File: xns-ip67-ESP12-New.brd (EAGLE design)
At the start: 65.3 x 139.1 mm, 86 parts, among them CN2 JSTPH, J1 DCJ0202, U2 MCP73831T-2ACI/OT, X1 ESP-12E

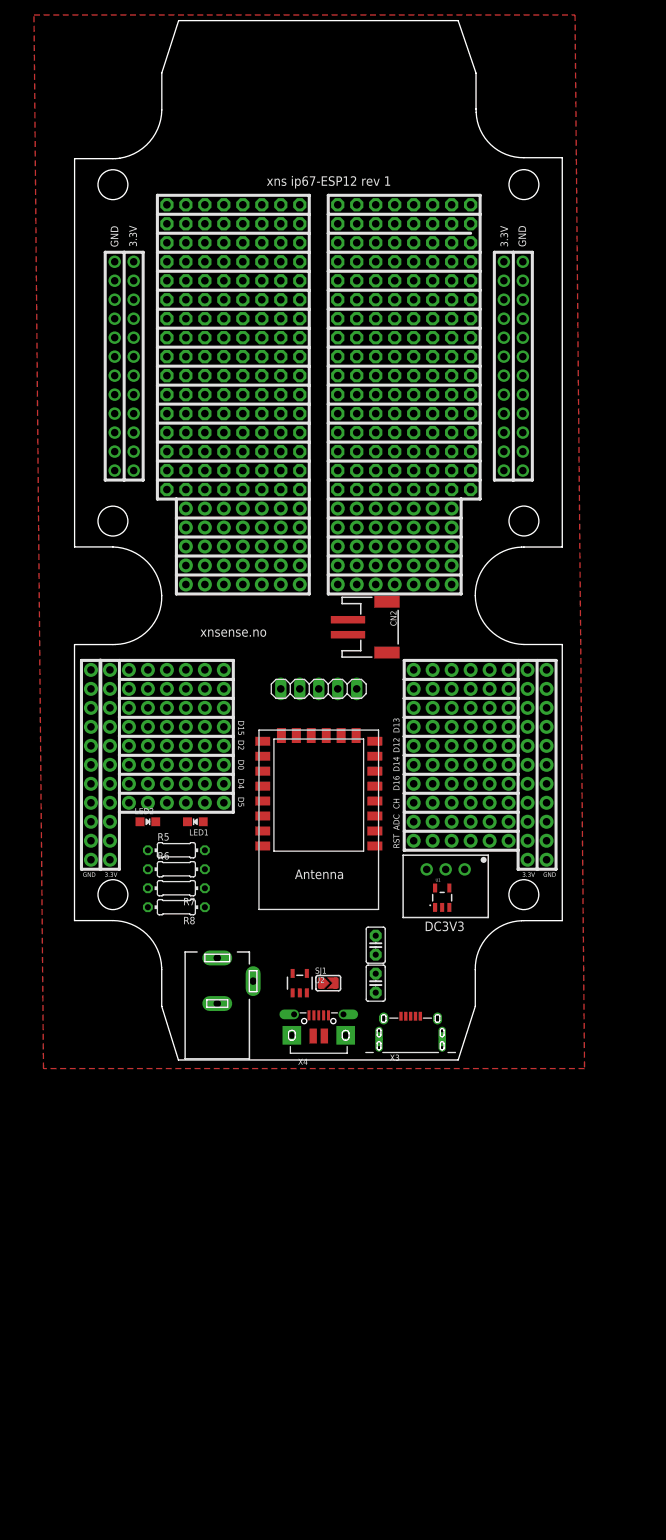
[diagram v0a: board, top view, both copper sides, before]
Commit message: ip67 version with A7, SIM, SMA
Test version with A7, SIM Card Holder and SMA Antenna
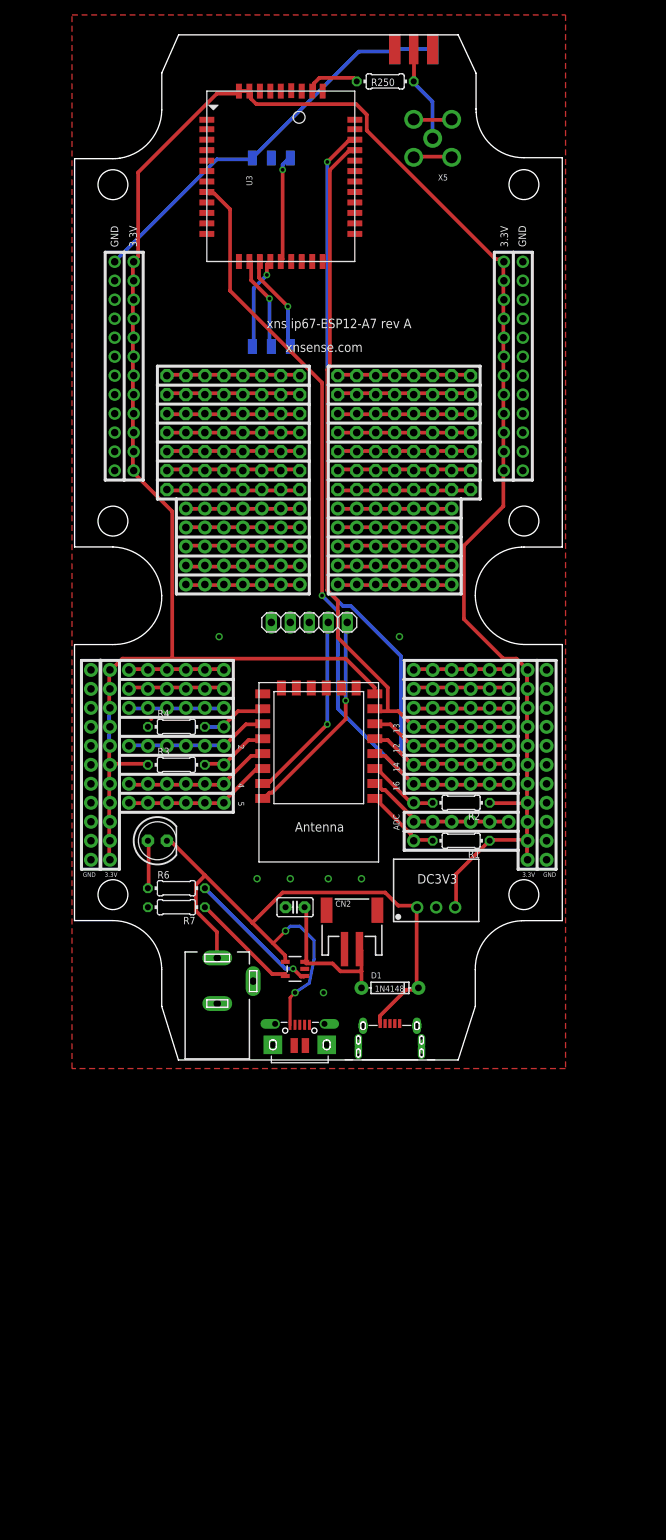
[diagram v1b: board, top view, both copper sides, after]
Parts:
- removed C3: 10uF, capacitor-wima:C2.5-2
- removed J11, J6, J8, J9: (no value), SparkFun-Connectors:1X06_NO_SILK
- removed JP16, JP17, JP18, JP19, JP20, JP21, JP22, JP23, JP24, JP5, JP6, JP7, JP8, JP9: (no value), adafruit:1X08-CLEANBIG
- removed LED1: RED, microbuilder:CHIPLED_0805_NOOUTLINE
- removed LED2: GREEN, microbuilder:CHIPLED_0805_NOOUTLINE
- removed R5: 470, eagle-ltspice:0204/7
- removed R8: 2.5k, eagle-ltspice:0204/7
- removed SJ1: (no value), microbuilder:SOLDERJUMPER_ARROW_NOPASTE
- removed U1: (no value), SparkFun-PowerIC:SOT23-5
- removed X4: (no value), microbuilder:4UCONN_20329_V2
- added D1: 1N4148, SparkFun-DiscreteSemi:DIODE-1N4148
- added JCB_MICROUSB: (no value), jcbrataas-2:USB-MICRO-B
- added LED4: Orange, adafruit:LED5MM
- added R1, R2, R3, R4: 10k, eagle-ltspice:0204/7
- added R250: (no value), eagle-ltspice:0204/7
- added SIMCARD: (no value), SparkFun-Connectors:SIMHOLDER
- added STD_MICROUSB: (no value), microbuilder:4UCONN_20329_V2
- added U3: A7, IC:A7
- added X5: (no value), adafruit:SMA90_DIP
- JP1, JP2, JP3, JP4: device adafruit:1X08-CLEANBIG -> adafruit:1X01-CLEANBIG
- R6: value 470 -> 470k
- X3: device jcbrataas:USB-MICRO-B -> adafruit:SMA_EDGELAUNCH
- moved X3 134.3 mm to (49.5, 138.4), turned to 270 degrees
- moved JP3 83.6 mm to (49.5, 30.5)
- moved JP4 76.3 mm to (49.5, 35.6)
- moved JP1 74.9 mm to (24.1, 40.6)
- moved JP2 67.3 mm to (24.1, 45.7)
- moved CN2 39.5 mm to (41.3, 19.7), turned to 0 degrees
- moved JP25 22.9 mm to (48.3, 80.0)
- moved JP26 22.9 mm to (48.3, 82.5)
- moved JP27 22.9 mm to (48.3, 85.1)
- moved JP28 22.9 mm to (48.3, 87.6)
- moved JP29 22.9 mm to (48.3, 90.2)
- moved JP30 22.9 mm to (48.3, 92.7)
- moved C4 11.9 mm to (33.7, 21.6), turned to 180 degrees
- moved JP37 8.98 mm to (35.6, 59.7)
- moved X1 6.35 mm to (36.8, 41.9)
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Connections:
- net N$13 renamed RX
- net N$4 renamed TX
- removed net N$25: JP5.1, JP5.2, JP5.3, JP5.4, JP5.5, JP5.6, JP5.7, JP5.8
- removed net N$26: JP6.1, JP6.2, JP6.3, JP6.4, JP6.5, JP6.6, JP6.7, JP6.8
- removed net N$27: JP7.1, JP7.2, JP7.3, JP7.4, JP7.5, JP7.6, JP7.7, JP7.8
- removed net N$28: JP8.1, JP8.2, JP8.3, JP8.4, JP8.5, JP8.6, JP8.7, JP8.8
- removed net N$29: JP9.1, JP9.2, JP9.3, JP9.4, JP9.5, JP9.6, JP9.7, JP9.8
- removed net N$42: JP24.1, JP24.2, JP24.3, JP24.4, JP24.5, JP24.6, JP24.7, JP24.8
- removed net N$43: JP22.1, JP22.2, JP22.3, JP22.4, JP22.5, JP22.6, JP22.7, JP22.8
- removed net N$44: JP21.1, JP21.2, JP21.3, JP21.4, JP21.5, JP21.6, JP21.7, JP21.8
- removed net N$45: JP20.1, JP20.2, JP20.3, JP20.4, JP20.5, JP20.6, JP20.7, JP20.8
- removed net N$46: JP19.1, JP19.2, JP19.3, JP19.4, JP19.5, JP19.6, JP19.7, JP19.8
- removed net N$47: JP18.1, JP18.2, JP18.3, JP18.4, JP18.5, JP18.6, JP18.7, JP18.8
- removed net N$48: JP17.1, JP17.2, JP17.3, JP17.4, JP17.5, JP17.6, JP17.7, JP17.8
- removed net N$49: JP16.1, JP16.2, JP16.3, JP16.4, JP16.5, JP16.6, JP16.7, JP16.8
- removed net N$5: J5.1, J5.2, J5.3, J5.4, J5.5, J5.6, X1.4
- removed net N$53: LED1.C, R5.1
- removed net N$57: R7.1, SJ1.2, U2.5
- removed net N$60: R8.1, SJ1.1
- removed net VBAT1: C4.1, CN2.2, U2.3
- removed net VDD: DC3V3.3, J15.1, J15.10, J15.11, J15.2, J15.3, J15.4, J15.5, J15.6, J15.7, J15.8, J15.9, J17.1, J17.10, J17.11, J17.2, J17.3, J17.4, J17.5, J17.6, J17.7, J17.8, J17.9, JP33.1, JP33.10, JP33.11, JP33.12, JP33.2, JP33.3, JP33.4, JP33.5, JP33.6, JP33.7, JP33.8, JP33.9, JP34.1, JP34.10, JP34.11, JP34.12, JP34.2, JP34.3, JP34.4, JP34.5, JP34.6, JP34.7, JP34.8, JP34.9, U1.5, X1.8
- removed net VDD1: C3.1, LED1.A, U2.4, X4.VBUS
- new net 3.3V: DC3V3.3, J15.1, J15.10, J15.11, J15.2, J15.3, J15.4, J15.5, J15.6, J15.7, J15.8, J15.9, J17.1, J17.10, J17.11, J17.2, J17.3, J17.4, J17.5, J17.6, J17.7, J17.8, J17.9, JP33.1, JP33.10, JP33.11, JP33.12, JP33.2, JP33.3, JP33.4, JP33.5, JP33.6, JP33.7, JP33.8, JP33.9, JP34.1, JP34.10, JP34.11, JP34.12, JP34.2, JP34.3, JP34.4, JP34.5, JP34.6, JP34.7, JP34.8, JP34.9, R1.1, R2.1, R3.1, U3.41, U3.42, X1.8
- new net N$13: SIMCARD.C3, U3.15
- new net N$4: X5.GND1, X5.GND2
- new net PWD_KEY: J5.1, J5.2, J5.3, J5.4, J5.5, J5.6, U3.8, X1.4
- new net RESET_KEY: U3.12
- new net UART_RX: J2.1, J2.2, J2.3, J2.4, J2.5, J2.6, U3.30, X1.7
- new net UART_TX: J4.1, J4.2, J4.3, J4.4, J4.5, J4.6, U3.31, X1.5
- new net V_BATT: C4.1, CN2.2, D1.A, U2.3
- net GND: now also JCB_MICROUSB.BL1, JCB_MICROUSB.BL2, JCB_MICROUSB.BL3, JCB_MICROUSB.BL4, JCB_MICROUSB.BR1, JCB_MICROUSB.BR2, JCB_MICROUSB.BR3, JCB_MICROUSB.BR4, JCB_MICROUSB.GND, JCB_MICROUSB.MTL1, JCB_MICROUSB.MTL2, JCB_MICROUSB.MTR1, JCB_MICROUSB.MTR2, R4.1, SIMCARD.C5, STD_MICROUSB.BASE@1, STD_MICROUSB.BASE@2, STD_MICROUSB.GND, STD_MICROUSB.SPRT@1, STD_MICROUSB.SPRT@2, STD_MICROUSB.SPRT@3, STD_MICROUSB.SPRT@4, U3.13, U3.18, U3.22, U3.25, U3.28, U3.34, U3.36, U3.39, U3.40, X3.GND@1, X3.GND@2, X3.GND@3, X3.GND@4; no longer C3.2, LED2.C, R8.2, U1.2, X3.BL1, X3.BL2, X3.BL3, X3.BR1, X3.BR2, X3.BR3, X3.GND, X3.MTL1, X3.MTL2, X3.MTR1, X3.MTR2, X4.BASE@1, X4.BASE@2, X4.GND, X4.SPRT@1, X4.SPRT@2, X4.SPRT@3, X4.SPRT@4
- net N$1: now also R250.1, U3.35; no longer J2.1, J2.2, J2.3, J2.4, J2.5, J2.6, X1.7
- net N$10: now also SIMCARD.C2, U3.14; no longer J9.1, J9.2, J9.3, J9.4, J9.5, J9.6, X1.10
- net N$12: now also JP1.1, R3.2; no longer J11.1, J11.2, J11.3, J11.4, J11.5, J11.6
- net N$21: now also JP3.1, R1.2, X1.1; no longer JP1.1, JP1.2, JP1.3, JP1.4, JP1.5, JP1.6, JP1.7, JP1.8
- net N$22: now also SIMCARD.C7, U3.17; no longer JP2.1, JP2.2, JP2.3, JP2.4, JP2.5, JP2.6, JP2.7, JP2.8
- net N$23: now also SIMCARD.C1, U3.16; no longer JP3.1, JP3.2, JP3.3, JP3.4, JP3.5, JP3.6, JP3.7, JP3.8
- net N$24: now also R7.1, U2.5; no longer JP4.1, JP4.2, JP4.3, JP4.4, JP4.5, JP4.6, JP4.7, JP4.8
- net N$3: now also R250.2, X3.P, X5.ANTENNA; no longer J4.1, J4.2, J4.3, J4.4, J4.5, J4.6, X1.5
- net N$55: no longer R5.2
- net N$59: now also LED4.A; no longer LED2.A
- net N$6: now also JP2.1, R4.2, X1.10; no longer J6.1, J6.2, J6.3, J6.4, J6.5, J6.6, X1.3
- net N$7: now also X5.GND3, X5.GND4; no longer JP23.1, JP23.2, JP23.3, JP23.4, JP23.5, JP23.6, JP23.7, JP23.8
- net N$9: now also JP4.1, R2.2, X1.3; no longer J8.1, J8.2, J8.3, J8.4, J8.5, J8.6, X1.1
- net VCC: now also D1.C, JCB_MICROUSB.VBUS, LED4.K, STD_MICROUSB.VBUS, U2.4; no longer U1.1, U1.3, X3.VBUS
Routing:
- net 3.3V: track 0.00 -> 311.4 mm
- net PWD_KEY: track 0.00 -> 111.2 mm, vias 0 -> 1
- net UART_TX: track 0.00 -> 111.0 mm, vias 0 -> 1
- net UART_RX: track 0.00 -> 99.3 mm
- net VCC: track 0.00 -> 99.1 mm, vias 0 -> 2
- net GND: track 0.00 -> 54.6 mm, vias 0 -> 7
- net TX: track 0.00 -> 28.5 mm, vias 0 -> 1
- net RX: track 0.00 -> 25.6 mm, vias 0 -> 1
- net V_BATT: track 0.00 -> 21.0 mm
- net N$8: track 0.00 -> 20.4 mm
- net N$14: track 0.00 -> 20.2 mm
- net N$15: track 0.00 -> 20.0 mm
- net N$11: track 0.00 -> 19.3 mm
- net N$2: track 0.00 -> 19.3 mm
- net N$31: track 0.00 -> 19.2 mm
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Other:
- board size 65.3 x 139.1 mm -> 65.3 x 137.2 mm
- board text added: "12"
- board text added: "13"
- board text added: "14"
- board text added: "16"
- board text added: "2"
- board text added: "4"
- board text added: "5"
- board text added: "xns ip67-ESP12-A7 rev A"
- board text added: "xnsense.com"
- board text removed: "CH"
- board text removed: "D0"
- board text removed: "D12"
- board text removed: "D13"
- board text removed: "D14"
- board text removed: "D15"
- board text removed: "D16"
- board text removed: "D2"
- board text removed: "D4"
- board text removed: "D5"
- board text removed: "RST"
- board text removed: "xns ip67-ESP12 rev 1"
- board text removed: "xnsense.no"

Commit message: More stuff
ff
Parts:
- removed DC3V3: R-78C1.8-1.0, dc-dc-converter:SIP3
- removed J10: (no value), SparkFun-Connectors:1X06_NO_SILK
- removed JP1, JP2, JP4: (no value), adafruit:1X01-CLEANBIG
- removed R2: 10k, eagle-ltspice:0204/7
- added C1: 1uF, microbuilder:0603-NO
- added C2, C3: 10µF, microbuilder:0805-NO
- added LED1: Red, adafruit:LED5MM
- added R12, R5: 10k, eagle-ltspice:0204/7
- added SW1, SW2: KMR2, microbuilder:BTN_KMR2_4.6X2.8
- added U1: (no value), microbuilder:SOT23-5
- added X2: (no value), adafruit:U.FL
- D1: value 1N4148 -> MBR120; device SparkFun-DiscreteSemi:DIODE-1N4148 -> microbuilder:SOD-123
- U2: device microbuilder:SOT23-5 -> microbuilder:SOT23-5@1
- moved D1 75.4 mm to (-1.27, -47.6)
- moved R3 59.8 mm to (76.8, 31.1)
- moved JP37 33.6 mm to (19.1, 30.5)
- moved LED4 29.1 mm to (21.0, 59.1)
- moved R250 7.62 mm to (45.7, 124.5)
- moved U3 6.48 mm to (30.5, 113.0)
- moved X5 6.02 mm to (50.2, 118.7)
- moved R1 5.08 mm to (55.9, 35.6), turned to 0 degrees
- moved SIMCARD 4.49 mm to (27.3, 109.9)
- renumbered R4 to R9
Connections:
- removed net N$11: J10.1, J10.2, J10.3, J10.4, J10.5, J10.6, X1.11
- removed net N$12: JP1.1, R3.2, X1.12
- removed net N$21: JP3.1, R1.2, X1.1
- removed net N$6: JP2.1, R9.2, X1.10
- removed net N$9: JP4.1, R2.2, X1.3
- new net CH_PD: R5.2, X1.3
- new net GPIO0: JP3.1, R12.2, SW2.B, SW2.B', X1.12
- new net GPIO02: X1.11
- new net GPIO15: R9.1, X1.10
- new net GPIO2: R3.2
- new net N$5: LED1.K, R12.1
- new net RESET: R1.2, SW1.B, SW1.B', X1.1
- net 3.3V: now also C1.1, C2.1, LED1.A, R5.1; no longer DC3V3.3, R2.1
- net GND: now also C1.2, C2.2, C3.2, R9.2, SW1.A, SW1.A', SW2.A, SW2.A', U1.2, X2.1, X2.2; no longer DC3V3.2, R9.1
- net N$3: now also X2.3
- net VCC: now also C3.1, U1.1, U1.3; no longer DC3V3.1
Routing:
- net 3.3V: track 311.4 -> 0.00 mm
- net PWD_KEY: track 111.2 -> 0.00 mm, vias 1 -> 0
- net UART_TX: track 111.0 -> 0.00 mm, vias 1 -> 0
- net UART_RX: track 99.3 -> 0.00 mm
- net VCC: track 99.1 -> 0.00 mm, vias 2 -> 0
- net GND: track 54.6 -> 0.00 mm, vias 7 -> 0
- net TX: track 28.5 -> 0.00 mm, vias 1 -> 0
- net RX: track 25.6 -> 0.00 mm, vias 1 -> 0
- net V_BATT: track 21.0 -> 0.00 mm
- net N$8: track 20.4 -> 0.00 mm
- net N$14: track 20.2 -> 0.00 mm
- net N$15: track 20.0 -> 0.00 mm
- net N$11: track 19.3 -> 0.00 mm
- net N$2: track 19.3 -> 0.00 mm
- net N$31: track 19.2 -> 0.00 mm
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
